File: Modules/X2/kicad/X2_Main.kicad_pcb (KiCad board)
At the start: 2 copper layers, 8.9 x 108.6 mm, 40 parts, among them U1 LM7321, U2 LM7321, U3 LM7321, U4 LM7321

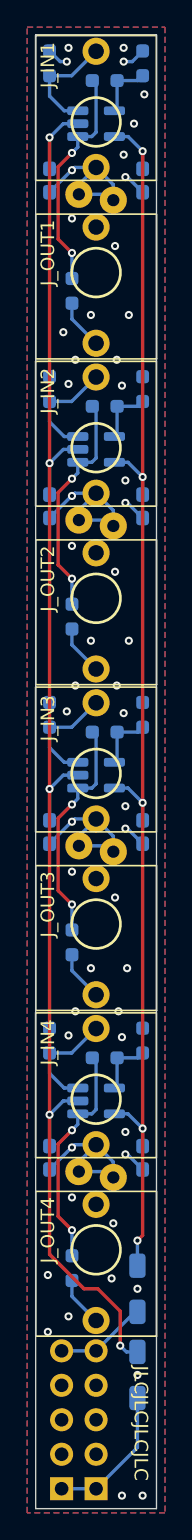
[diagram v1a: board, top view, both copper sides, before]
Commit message: Update X2 to new version.
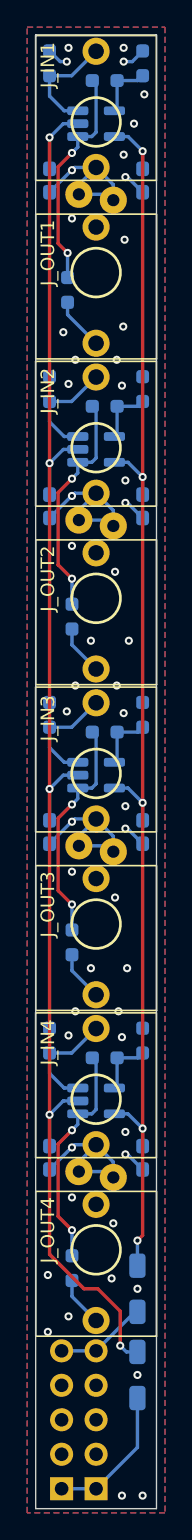
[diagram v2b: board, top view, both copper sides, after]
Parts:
- added REF**: JLCPCB_QR_5mm, Eurorack:JLCPCB_QR_5mm, B.Cu at (90.4, 53.0)
- moved R1 0.33 mm to (86.8, 53.4)
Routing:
- net GND: vias 53 -> 52
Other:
- board text added: "X2 v1.1"
- board text removed: "JLCJLCJLCJLC"
- board text removed: "X2 v1.0"
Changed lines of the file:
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@@
 	(paper "A4")
 	(title_block
-		(rev "v1.0")
+		(rev "v1.1")
 	)
 	(layers
@@
 		)
 	)
+	(footprint "Eurorack:JLCPCB_QR_5mm"
+		(layer "B.Cu")
+		(at 90.4 53 180)
+		(property "Reference" "REF**"
+			(at 0 0.5 0)
+			(unlocked yes)
+			(layer "B.SilkS")
+			(hide yes)
+			(effects
+				(font
+					(size 1 1)
+					(thickness 0.1)
+				)
+				(justify mirror)
+			)
+		)
+		(property "Value" "JLCPCB_QR_5mm"
+			(at 0 -1 0)
+			(unlocked yes)
+			(layer "B.Fab")
+			(effects
+				(font
+					(size 1 1)
+					(thickness 0.15)
+				)
+				(justify mirror)
+			)
+		)
+		(property "Footprint" "Eurorack:JLCPCB_QR_5mm"
+			(at 0 0 0)
+			(unlocked yes)
+			(layer "B.Fab")
+			(hide yes)
+			(effects
+				(font
+					(size 1 1)
+					(thickness 0.15)
+				)
+				(justify mirror)
+			)
+		)
+		(property "Datasheet" ""
+			(at 0 0 0)
+			(unlocked yes)
+			(layer "B.Fab")
+			(hide yes)
+			(effects
+				(font
+					(size 1 1)
+					(thickness 0.15)
+				)
+				(justify mirror)
+			)
+		)
+		(property "Description" ""
+			(at 0 0 0)
+			(unlocked yes)
+			(layer "B.Fab")
+			(hide yes)
+			(effects
+				(font
+					(size 1 1)
+					(thickness 0.15)
+				)
+				(justify mirror)
+			)
+		)
+		(fp_rect
+			(start 2.5 -2.5)
+			(end -2.5 2.5)
+			(stroke
+				(width 0)
+				(type solid)
+			)
+			(fill solid)
+			(layer "B.SilkS")
+		)
+		(fp_text user "${REFERENCE}"
+			(at 0 -2.5 0)
+			(unlocked yes)
+			(layer "B.Fab")
+			(effects
+				(font
+					(size 1 1)
+					(thickness 0.15)
+				)
+				(justify mirror)
+			)
+		)
+	)
 	(footprint "Resistor_SMD:R_0603_1608Metric_Pad0.98x0.95mm_HandSolder"
 		(layer "B.Cu")
@@
 	(footprint "Resistor_SMD:R_0603_1608Metric_Pad0.98x0.95mm_HandSolder"
 		(layer "B.Cu")
-		(at 87.122 53.467 90)
+		(at 86.8 53.4 90)
 		(descr "Resistor SMD 0603 (1608 Metric), square (rectangular) end terminal, IPC_7351 nominal with elongated pad for handsoldering. (Body size source: IPC-SM-782 page 72, https://www.pcb-3d.com/wordpress/wp-content/uploads/ipc-sm-782a_amendment_1_and_2.pdf), generated with kicad-footprint-generator")
 		(tags "resistor handsolder")
@@
 		(attr through_hole)
 		(fp_line
-			(start -1.586 -5.715)
-			(end -4.064 -5.715)
+			(start -1.6368 -5.6896)
+			(end -3.81 -5.6896)
 			(stroke
 				(width 0.5)
@@
 			(layer "B.SilkS")
 		)
+		(fp_rect
+			(start 6.27 -8.75)
+			(end -3.73 8.75)
+			(stroke
+				(width 0.1)
+				(type solid)
+			)
+			(fill none)
+			(layer "User.7")
+		)
 		(fp_text user "RED"
 			(at -2.032 -2.286 90)
@@
 		(layer "User.6")
 	)
-	(gr_text "X2 v1.0"
+	(gr_text "X2 v1.1"
 		(at 92.205 77.724 90)
 		(layer "B.SilkS")
@@
 		)
 	)
-	(gr_text "JLCJLCJLCJLC"
-		(at 92.202 136.906 -90)
-		(layer "F.SilkS")
-		(effects
-			(font
-				(size 1 1)
-				(thickness 0.15)
-			)
-		)
-	)
 	(via
 		(at 90.805 108.458)
@@
 	)
 	(via
-		(at 91.313 55.245)
+		(at 90.9 56.1)
 		(size 0.6)
 		(drill 0.3)
@@
 	)
 	(via
-		(at 88.519 55.245)
-		(size 0.6)
-		(drill 0.3)
-		(layers "F.Cu" "B.Cu")
-		(free yes)
-		(net 1)
-	)
-	(via
-		(at 90.297 50.165)
+		(at 91 49.7)
 		(size 0.6)
 		(drill 0.3)
@@
 	)
 	(segment
-		(start 87.122 55.55)
+		(start 86.8 55.228)
 		(end 88.9 57.328)
 		(width 0.25)
@@
 	)
 	(segment
-		(start 87.122 54.3795)
-		(end 87.122 55.55)
+		(start 86.8 54.3125)
+		(end 86.8 55.228)
 		(width 0.25)
 		(layer "B.Cu")
@@
 	)
 	(segment
-		(start 86.106 49.657)
-		(end 87.122 50.673)
+		(start 86.106 44.323)
+		(end 87.122 43.307)
 		(width 0.25)
 		(layer "F.Cu")
@@
 	)
 	(segment
-		(start 87.122 43.307)
+		(start 86.106 49.979)
 		(end 86.106 44.323)
 		(width 0.25)
@@
 	)
 	(segment
-		(start 86.106 44.323)
-		(end 86.106 49.657)
+		(start 86.8 50.673)
+		(end 86.106 49.979)
 		(width 0.25)
 		(layer "F.Cu")
@@
 	)
 	(via
-		(at 87.122 50.673)
+		(at 86.8 50.673)
 		(size 0.6)
 		(drill 0.3)
@@
 	)
 	(segment
-		(start 87.122 50.673)
-		(end 87.122 52.5545)
+		(start 87.55 42.098)
+		(end 88.585 42.098)
 		(width 0.25)
 		(layer "B.Cu")
@@
 	)
 	(segment
-		(start 87.55 42.098)
-		(end 88.585 42.098)
+		(start 87.122 43.307)
+		(end 87.55 42.879)
 		(width 0.25)
 		(layer "B.Cu")
@@
 	)
 	(segment
-		(start 87.122 43.307)
-		(end 87.55 42.879)
+		(start 86.8 50.673)
+		(end 86.8 52.4875)
 		(width 0.25)
 		(layer "B.Cu")
